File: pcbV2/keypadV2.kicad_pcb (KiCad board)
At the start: 2 copper layers, 93.7 x 93.3 mm, 55 parts, among them J3 Conn_01x03_Male, J6 Conn_01x03_Male, Q1 Q_NMOS_GSD, Q2 Q_NMOS_GSD, SW1 SW_Push, SW10 SW_Push, SW11 SW_Push, SW12 SW_Push, SW14 SW_Push, SW15 SW_Push, SW16 SW_Push, SW17 SW_DIP_x03, SW2 SW_Push, SW3 SW_Push, SW4 SW_Push, SW5 SW_Push, SW6 SW_Push, SW7 SW_Push, SW8 SW_Push, SW9 SW_Push, U1 Teensy4.0, U2 Waveshare_OLED_RGB

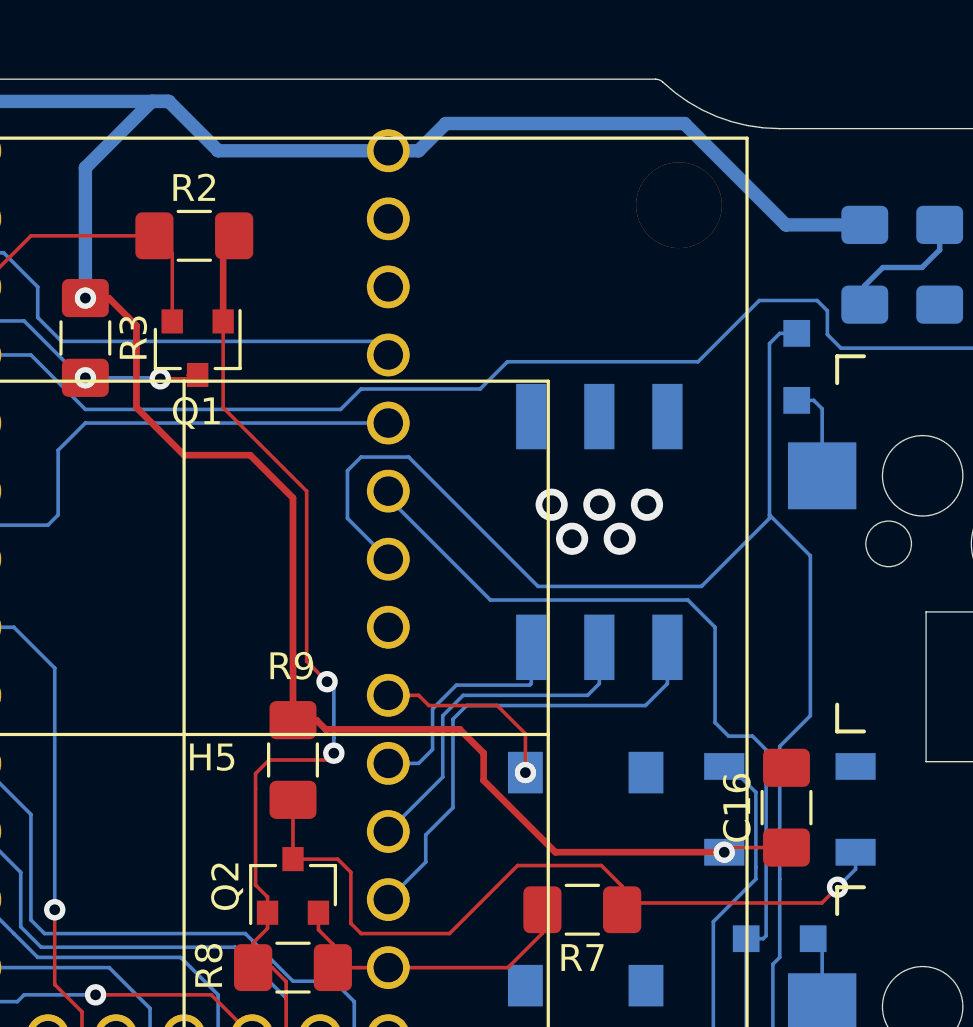
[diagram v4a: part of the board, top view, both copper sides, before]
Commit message: moved some labels around
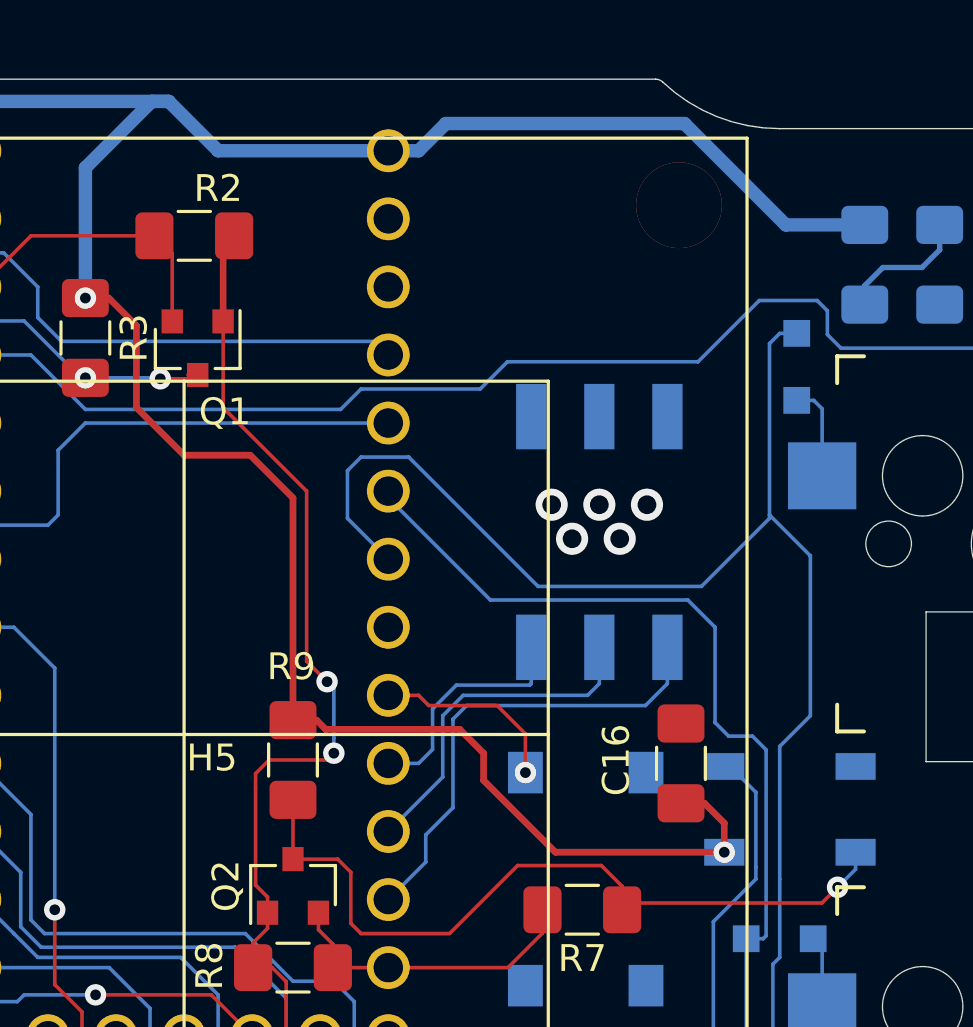
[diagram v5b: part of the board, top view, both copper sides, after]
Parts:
- moved C16 4.27 mm to (200.4, 69.1)
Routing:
- net +5V: track 322.4 -> 323.2 mm
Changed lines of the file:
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@@
     (thickness 1.6)
     (drawings 64)
-    (tracks 628)
+    (tracks 630)
     (zones 0)
     (modules 55)
@@
     (35 F.Paste user)
     (36 B.SilkS user)
-    (37 F.SilkS user hide)
+    (37 F.SilkS user)
     (38 B.Mask user)
     (39 F.Mask user)
@@
   )
   (setup
-    (last_trace_width 0.135)
+    (last_trace_width 0.25)
     (user_trace_width 0.135)
     (user_trace_width 0.2)
@@
   )
   (module Capacitor_SMD:C_1206_3216Metric_Pad1.42x1.75mm_HandSolder (layer F.Cu)
-    (at 204.343 70.739 90)
+    (at 200.406 69.088 90)
     (descr "Capacitor SMD 1206 (3216 Metric), square (rectangular) end terminal, IPC_7351 nominal with elongated pad for handsoldering. (Body size source: http://www.tortai-tech.com/upload/download/2011102023233369053.pdf), generated with kicad-footprint-generator")
     (tags "capacitor handsolder")
     (attr smd)
-    (fp_text reference C16 (at 0 -1.82 270) (layer F.SilkS)
+    (fp_text reference C16 (at 0.127 -2.413 270) (layer F.SilkS)
       (effects (font (size 1 1) (thickness 0.15)))
     )
@@
     (tags SOT-23)
     (attr smd)
-    (fp_text reference Q1 (at 2.3749 0.0254) (layer F.SilkS)
+    (fp_text reference Q1 (at 2.3749 -1.016) (layer F.SilkS)
       (effects (font (size 1 1) (thickness 0.15)))
     )
@@
     (tags "resistor handsolder")
     (attr smd)
-    (fp_text reference R2 (at 0 1.7653 180) (layer F.SilkS)
+    (fp_text reference R2 (at -0.889 1.7653 180) (layer F.SilkS)
       (effects (font (size 1 1) (thickness 0.15)))
     )
@@
   (segment (start 139.96162 87.63762) (end 139.96162 66.31812) (width 0.5) (layer B.Cu) (net 2))
   (via (at 202.02 72.4025) (size 0.8) (drill 0.4) (layers F.Cu B.Cu) (net 2))
-  (segment (start 204.343 72.2265) (end 202.196 72.2265) (width 0.135) (layer F.Cu) (net 2))
   (segment (start 202.196 72.2265) (end 202.02 72.4025) (width 0.135) (layer F.Cu) (net 2))
   (segment (start 179.056 51.7255) (end 180.086 52.7555) (width 0.25) (layer F.Cu) (net 2))
@@
   (segment (start 193.04 68.707) (end 193.04 69.723) (width 0.25) (layer F.Cu) (net 2))
   (segment (start 187.1475 67.818) (end 192.151 67.818) (width 0.25) (layer F.Cu) (net 2))
+  (segment (start 202.02 71.3145) (end 202.02 72.4025) (width 0.25) (layer F.Cu) (net 2))
+  (segment (start 200.406 70.5755) (end 201.281 70.5755) (width 0.25) (layer F.Cu) (net 2))
+  (segment (start 201.281 70.5755) (end 202.02 71.3145) (width 0.25) (layer F.Cu) (net 2))
   (segment (start 142.935 56.9715) (end 142.2908 56.3273) (width 0.135) (layer B.Cu) (net 3))
   (segment (start 142.935 58.3565) (end 142.935 56.9715) (width 0.135) (layer B.Cu) (net 3))

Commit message: generated plots files
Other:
- board text added: "lazy-board v2.0 [2020]"
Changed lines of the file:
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@@
   (general
     (thickness 1.6)
-    (drawings 64)
+    (drawings 68)
     (tracks 630)
     (zones 0)
@@
       (usegerberadvancedattributes false)
       (creategerberjobfile false)
-      (excludeedgelayer true)
+      (excludeedgelayer false)
       (linewidth 0.100000)
       (plotframeref false)
@@
       (outputformat 1)
       (mirror false)
-      (drillshape 1)
+      (drillshape 0)
       (scaleselection 1)
-      (outputdirectory ""))
+      (outputdirectory "plots/"))
   )
   (net 0 "")
@@
     )
   )
-  (dimension 46.863007 (width 0.12) (layer F.SilkS)
-    (gr_text "46.863 mm" (at 158.466267 17.569033 359.9689454) (layer F.SilkS)
-      (effects (font (size 1 1) (thickness 0.15)))
-    )
-    (feature1 (pts (xy 181.864 79.883) (xy 181.897397 18.265312)))
-    (feature2 (pts (xy 135.001 79.8576) (xy 135.034397 18.239912)))
-    (crossbar (pts (xy 135.034079 18.826333) (xy 181.897079 18.851733)))
-    (arrow1a (pts (xy 181.897079 18.851733) (xy 180.770258 19.437543)))
-    (arrow1b (pts (xy 181.897079 18.851733) (xy 180.770893 18.264702)))
-    (arrow2a (pts (xy 135.034079 18.826333) (xy 136.160265 19.413364)))
-    (arrow2b (pts (xy 135.034079 18.826333) (xy 136.1609 18.240523)))
+  (gr_line (start 177.038 85.217) (end 187.198 85.217) (layer B.SilkS) (width 0.12))
+  (gr_line (start 177.038 81.407) (end 177.038 85.217) (layer B.SilkS) (width 0.12))
+  (gr_line (start 187.198 81.407) (end 177.038 81.407) (layer B.SilkS) (width 0.12))
+  (gr_line (start 187.198 85.217) (end 187.198 81.407) (layer B.SilkS) (width 0.12))
+  (gr_text "lazy-board \nv2.0 [2020]" (at 182.118 83.312) (layer B.SilkS)
+    (effects (font (size 1 1) (thickness 0.15)) (justify mirror))
   )
   (gr_line (start 181.864 105.0925) (end 181.864 34.3535) (layer Cmts.User) (width 0.12))

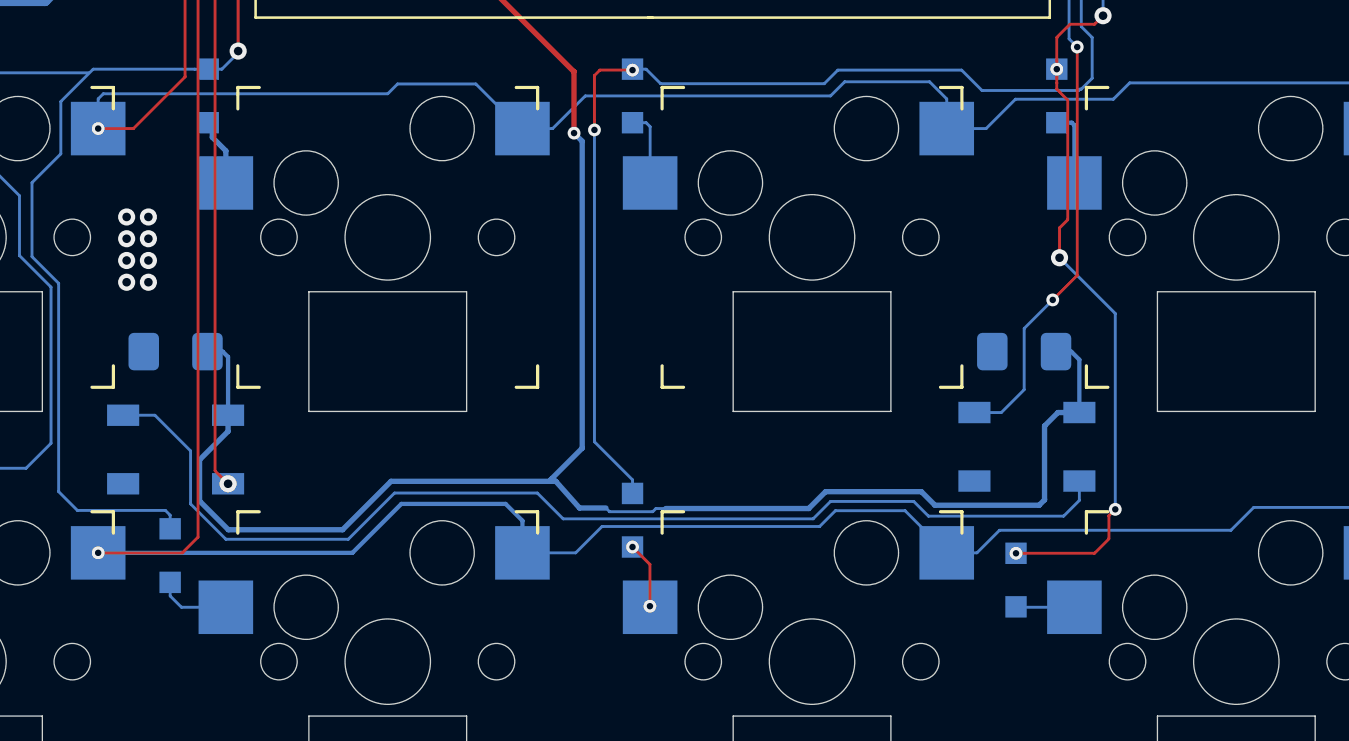
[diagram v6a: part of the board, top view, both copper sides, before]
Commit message: updating daughter board to be more structurally safe
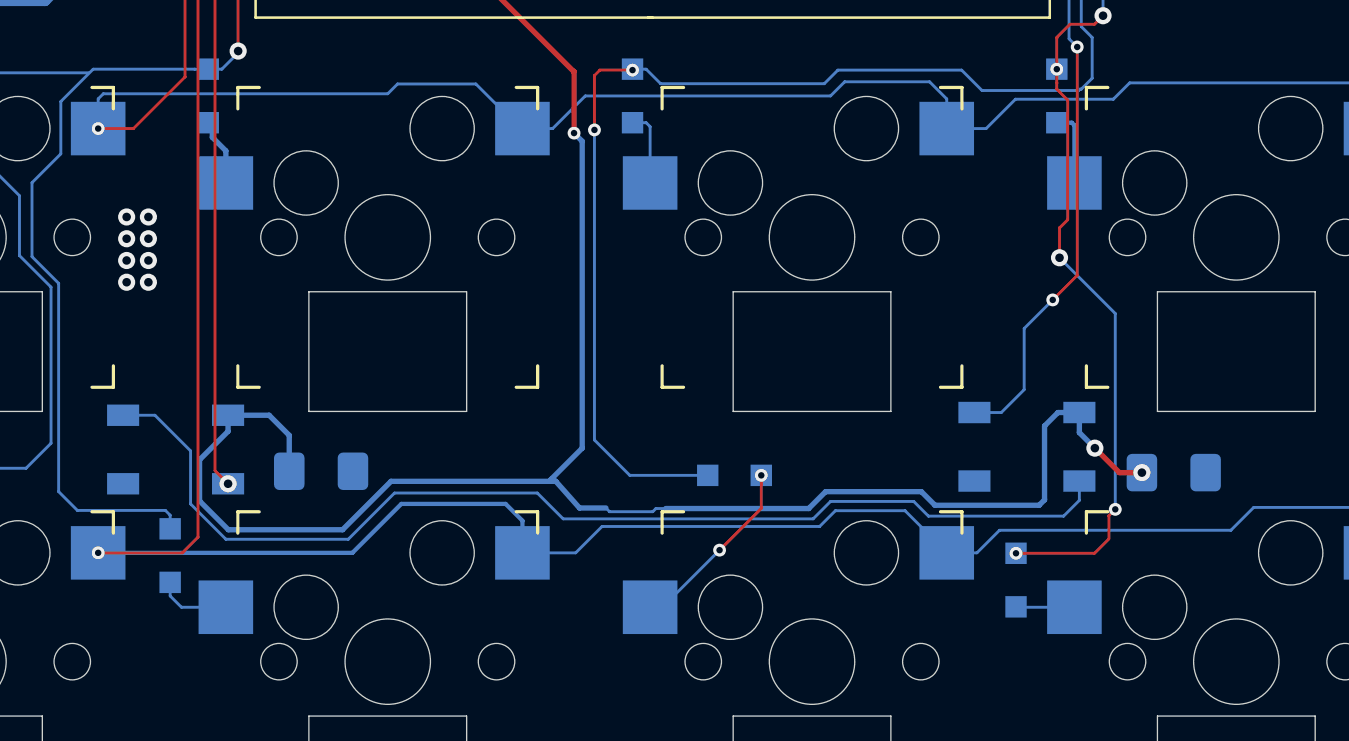
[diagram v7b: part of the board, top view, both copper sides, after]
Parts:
- moved C15 8.98 mm to (208.7, 111.5), turned to 0 degrees
- moved C14 8.80 mm to (168.8, 111.4), turned to 0 degrees
- moved D11 5.20 mm to (188.2, 111.6), turned to 0 degrees
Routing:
- net Net-(D11-Pad2): track 3.10 -> 8.65 mm
- net COL3: track 91.1 -> 93.9 mm
- net +5V: track 323.2 -> 325.3 mm, vias 7 -> 9
